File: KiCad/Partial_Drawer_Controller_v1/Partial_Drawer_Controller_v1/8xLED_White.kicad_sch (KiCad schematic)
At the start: 17 parts, among them Q38 AO3400A, Q39 AO3401A

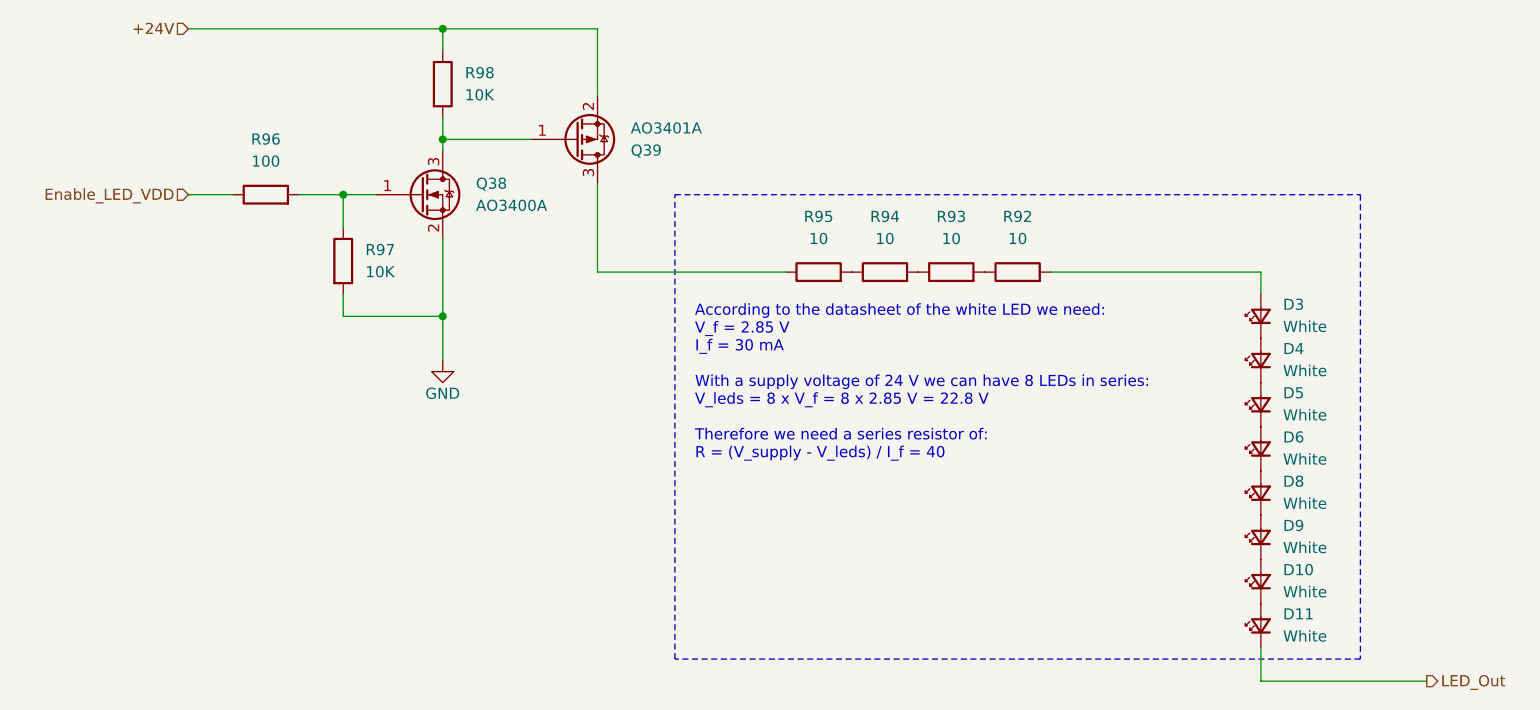
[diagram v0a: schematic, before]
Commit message: feat: finished LED control
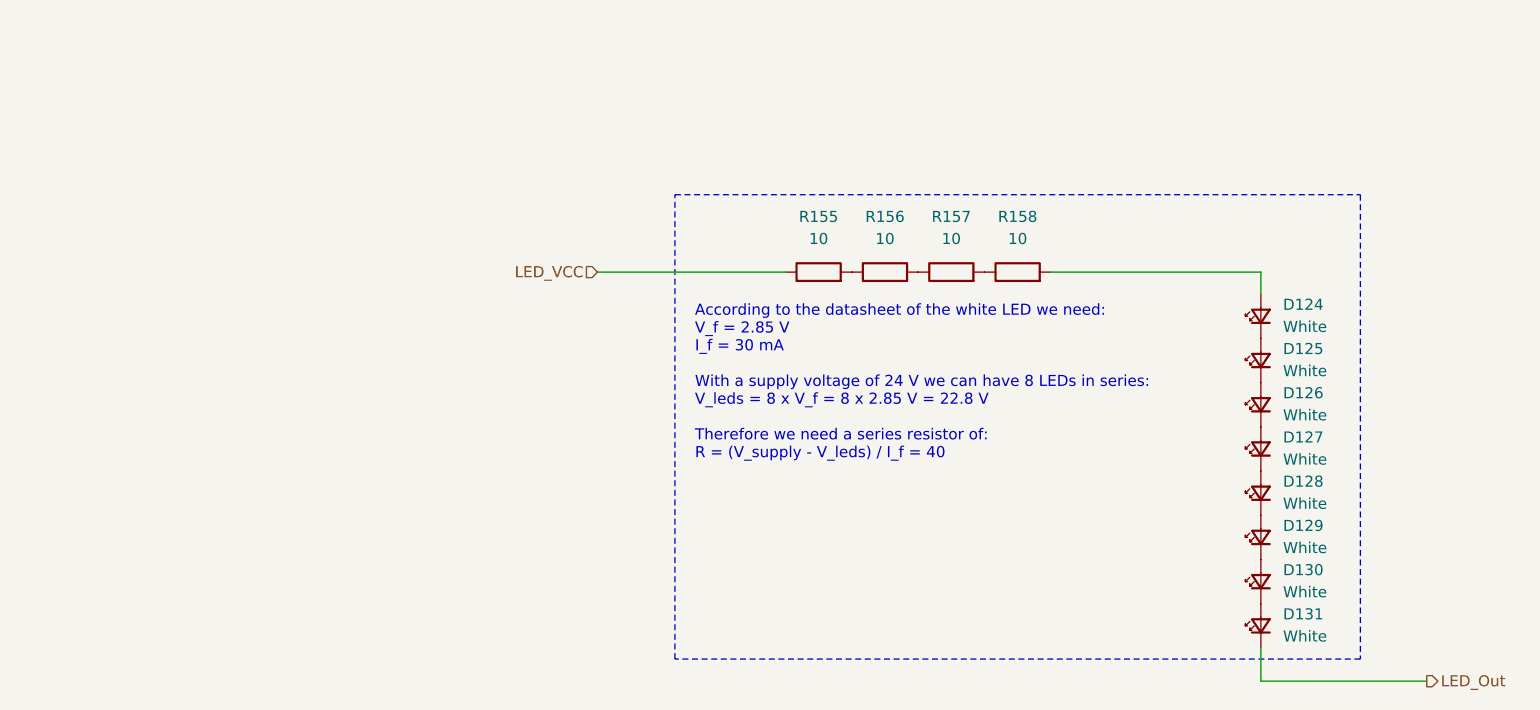
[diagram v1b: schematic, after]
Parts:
- removed Q38: AO3400A, Package_TO_SOT_SMD:SOT-23, symbol _Transistor_FET:AO3400A
- removed Q39: AO3401A, Package_TO_SOT_SMD:SOT-23, symbol _Transistor_FET:AO3401A
- removed R96: 100, Resistor_SMD:R_0402_1005Metric, symbol _R_0402:100
- removed R97, R98: 10K, Resistor_SMD:R_0402_1005Metric, symbol _R_0402:10K
- renumbered D3 to D124, D4 to D125, D5 to D126, D6 to D127, D8 to D128, D9 to D129, D10 to D130, D11 to D131, R95 to R155, R94 to R156, R93 to R157, R92 to R158
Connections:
- net LED_VCC: now reaches R155.1

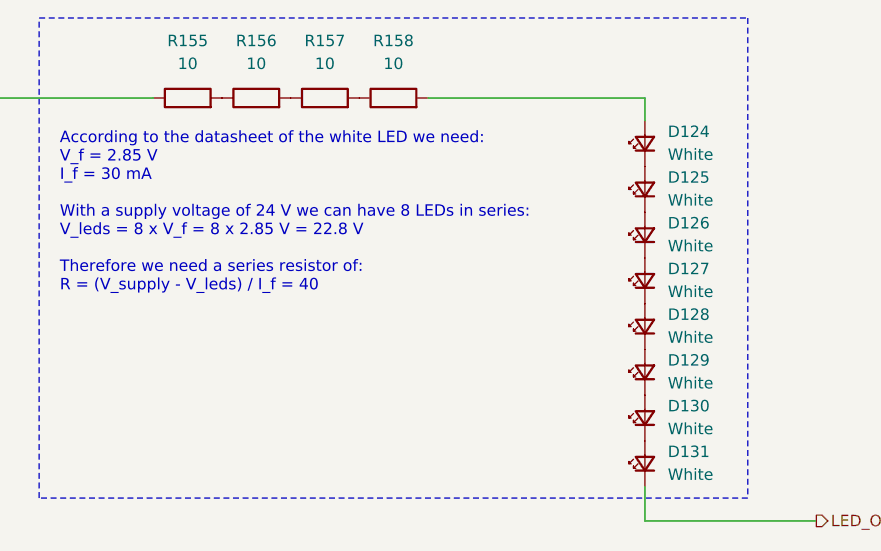
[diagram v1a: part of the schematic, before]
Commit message: feat: adds a lot of connectors and e-drawer support
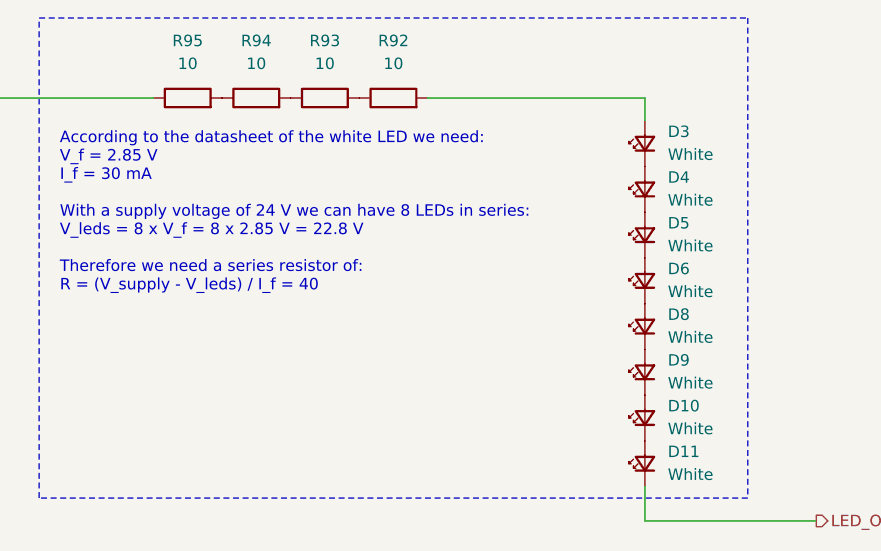
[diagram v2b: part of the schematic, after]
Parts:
- renumbered D130 to D10, D131 to D11, D124 to D3, D125 to D4, D126 to D5, D127 to D6, D128 to D8, D129 to D9, R158 to R92, R157 to R93, R156 to R94, R155 to R95

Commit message: feat: adds mounting holes
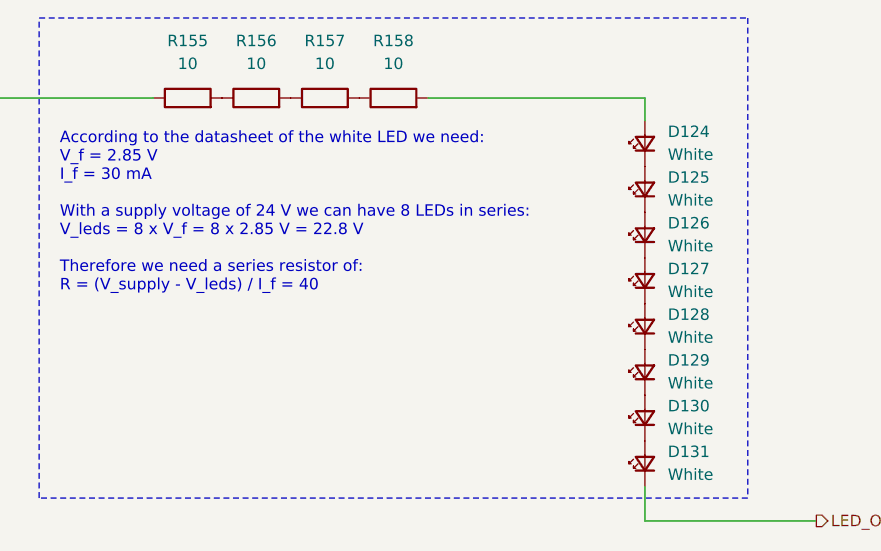
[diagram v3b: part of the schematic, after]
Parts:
- renumbered D3 to D124, D4 to D125, D5 to D126, D6 to D127, D8 to D128, D9 to D129, D10 to D130, D11 to D131, R95 to R155, R94 to R156, R93 to R157, R92 to R158

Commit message: feat: more progress in placing other parts
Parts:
- renumbered D130 to D10, D131 to D11, D124 to D3, D125 to D4, D126 to D5, D127 to D6, D128 to D8, D129 to D9, R158 to R92, R157 to R93, R156 to R94, R155 to R95

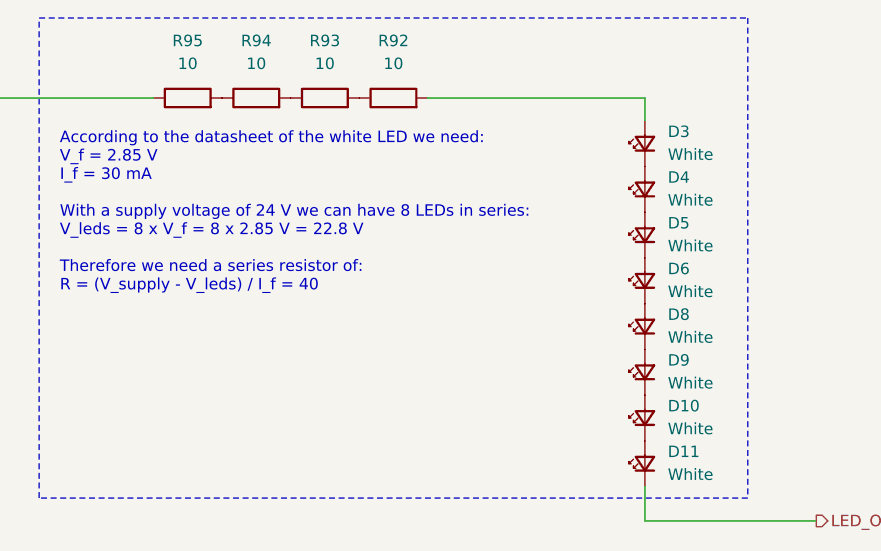
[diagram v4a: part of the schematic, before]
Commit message: feat: first progress in routing layers
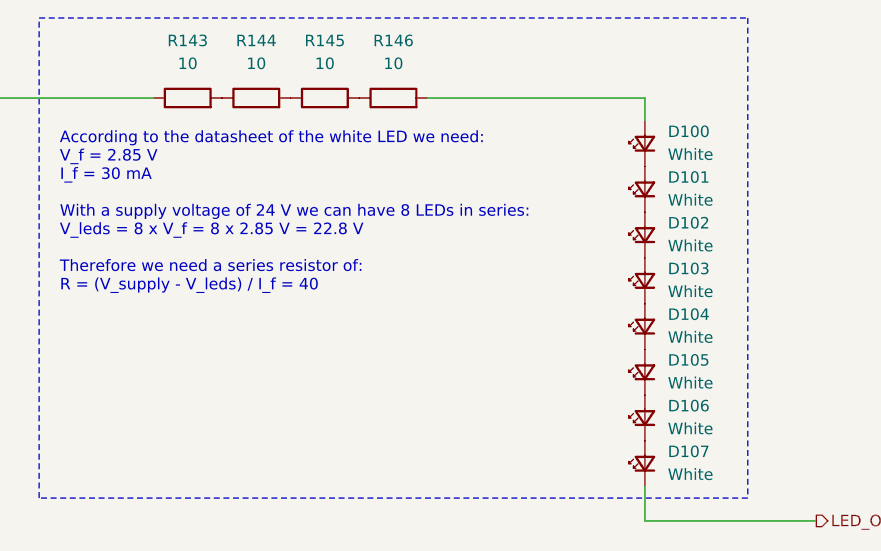
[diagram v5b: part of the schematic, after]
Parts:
- renumbered D3 to D100, D4 to D101, D5 to D102, D6 to D103, D8 to D104, D9 to D105, D10 to D106, D11 to D107, R95 to R143, R94 to R144, R93 to R145, R92 to R146

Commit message: feat: small changes and creates manufacturing files
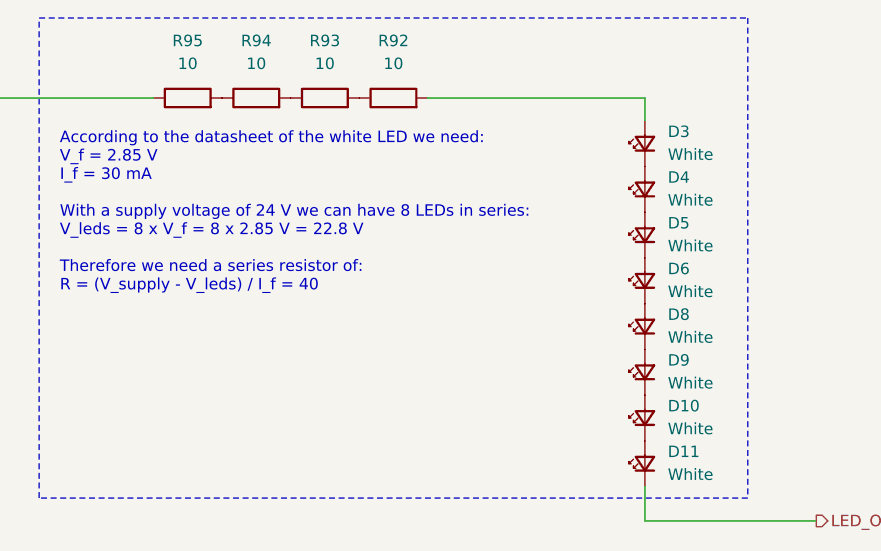
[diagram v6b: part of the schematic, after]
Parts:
- renumbered D106 to D10, D107 to D11, D100 to D3, D101 to D4, D102 to D5, D103 to D6, D104 to D8, D105 to D9, R146 to R92, R145 to R93, R144 to R94, R143 to R95

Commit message: feat: minor adjustments and new export of manufacturing files for `Partial_Drawer_controller_v1`
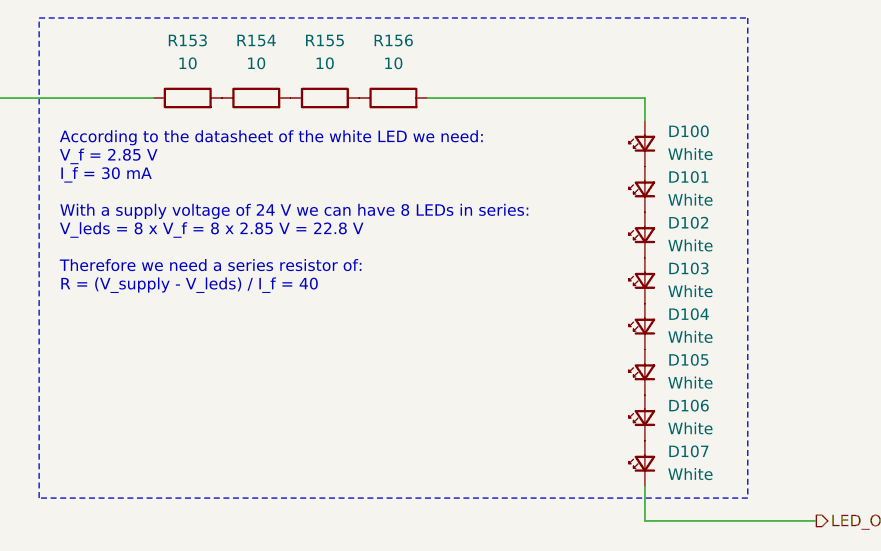
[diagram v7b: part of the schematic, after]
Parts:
- renumbered D3 to D100, D4 to D101, D5 to D102, D6 to D103, D8 to D104, D9 to D105, D10 to D106, D11 to D107, R95 to R153, R94 to R154, R93 to R155, R92 to R156

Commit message: feat: replaces `CP_Elec_12.5x13.5` with `CP_Elec_10x10` for `Partial_Drawer_Controller_v1`
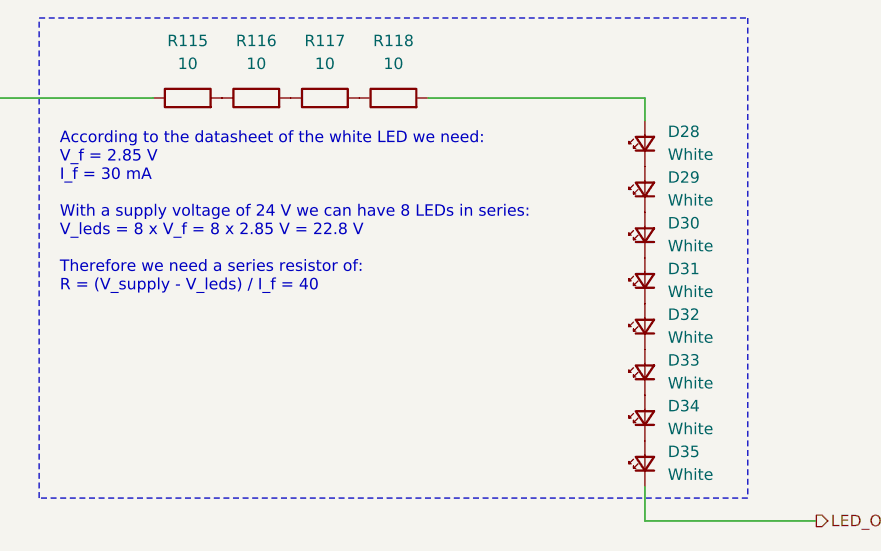
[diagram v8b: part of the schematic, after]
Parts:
- renumbered D100 to D28, D101 to D29, D102 to D30, D103 to D31, D104 to D32, D105 to D33, D106 to D34, D107 to D35, R153 to R115, R154 to R116, R155 to R117, R156 to R118
